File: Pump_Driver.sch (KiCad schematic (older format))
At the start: 6 parts

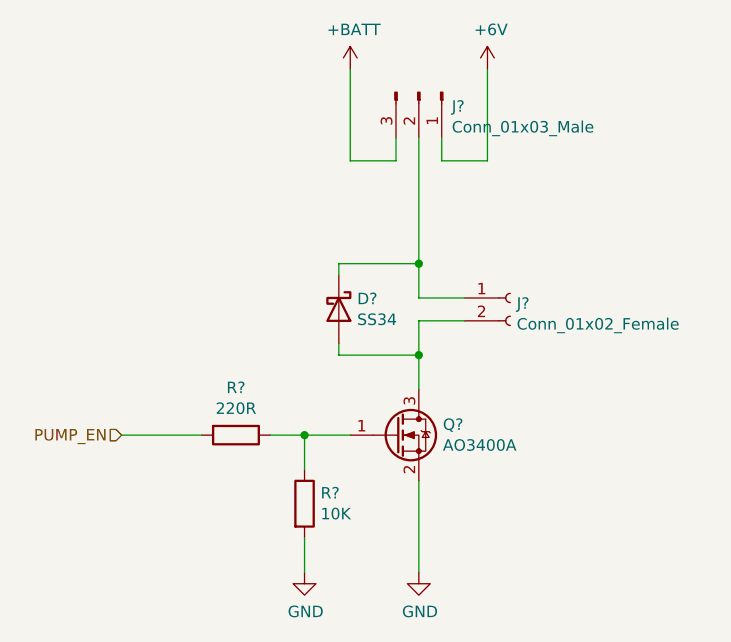
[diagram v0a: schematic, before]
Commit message: Add MPPT battery charger and polyfuse, replace reverse polarity
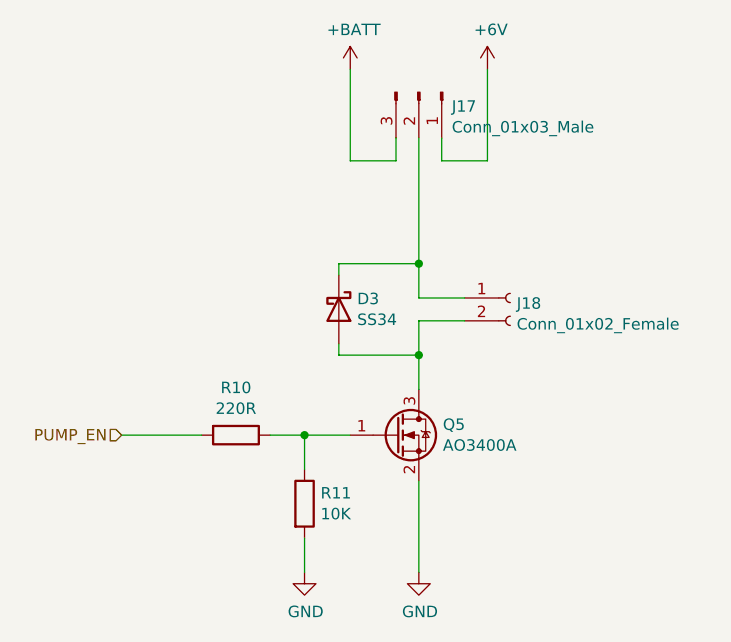
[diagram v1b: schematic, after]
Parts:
- gave numbers to parts that had none: 6
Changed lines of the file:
@@
 PUMP_EN
 $Comp
-L Transistor_FET:AO3400A Q?
+L Transistor_FET:AO3400A Q5
 U 1 1 60BE5370
 P 5950 4250
-F 0 "Q?" H 6155 4296 50  0000 L CNN
+F 0 "Q5" H 6155 4296 50  0000 L CNN
 F 1 "AO3400A" H 6155 4205 50  0000 L CNN
 F 2 "Package_TO_SOT_SMD:SOT-23" H 6150 4175 50  0001 L CIN
@@
 $EndComp
 $Comp
-L Device:R R?
+L Device:R R10
 U 1 1 60BEC7F4
 P 5250 4250
-F 0 "R?" V 5043 4250 50  0000 C CNN
+F 0 "R10" V 5043 4250 50  0000 C CNN
 F 1 "220R" V 5134 4250 50  0000 C CNN
 F 2 "" V 5180 4250 50  0001 C CNN
@@
 	5400 4250 5550 4250
 $Comp
-L Device:R R?
+L Device:R R11
 U 1 1 60BEDCBD
 P 5550 4550
-F 0 "R?" H 5620 4596 50  0000 L CNN
+F 0 "R11" H 5620 4596 50  0000 L CNN
 F 1 "10K" H 5620 4505 50  0000 L CNN
 F 2 "" V 5480 4550 50  0001 C CNN
@@
 	5550 4250 5750 4250
 $Comp
-L power:GND #PWR?
+L power:GND #PWR039
 U 1 1 60BEE60C
 P 5550 4850
-F 0 "#PWR?" H 5550 4600 50  0001 C CNN
+F 0 "#PWR039" H 5550 4600 50  0001 C CNN
 F 1 "GND" H 5555 4677 50  0000 C CNN
 F 2 "" H 5550 4850 50  0001 C CNN
@@
 	5550 4850 5550 4700
 $Comp
-L power:GND #PWR?
+L power:GND #PWR041
 U 1 1 60BEEC8C
 P 6050 4850
-F 0 "#PWR?" H 6050 4600 50  0001 C CNN
+F 0 "#PWR041" H 6050 4600 50  0001 C CNN
 F 1 "GND" H 6055 4677 50  0000 C CNN
 F 2 "" H 6050 4850 50  0001 C CNN
@@
 	6050 4850 6050 4450
 $Comp
-L Connector:Conn_01x02_Female J?
+L Connector:Conn_01x02_Female J18
 U 1 1 60BF29BF
 P 6450 3650
-F 0 "J?" H 6478 3626 50  0000 L CNN
+F 0 "J18" H 6478 3626 50  0000 L CNN
 F 1 "Conn_01x02_Female" H 6478 3535 50  0000 L CNN
 F 2 "" H 6450 3650 50  0001 C CNN
@@
 $EndComp
 $Comp
-L Connector:Conn_01x03_Male J?
+L Connector:Conn_01x03_Male J17
 U 1 1 60BF35EE
 P 6050 2750
-F 0 "J?" V 6112 2894 50  0000 L CNN
+F 0 "J17" V 6112 2894 50  0000 L CNN
 F 1 "Conn_01x03_Male" V 6203 2894 50  0000 L CNN
 F 2 "" H 6050 2750 50  0001 C CNN
@@
 	6050 3650 6050 3500
 $Comp
-L Device:D_Schottky D?
+L Device:D_Schottky D3
 U 1 1 60BF7F76
 P 5700 3700
-F 0 "D?" V 5654 3780 50  0000 L CNN
+F 0 "D3" V 5654 3780 50  0000 L CNN
 F 1 "SS34" V 5745 3780 50  0000 L CNN
 F 2 "Diode_SMD:D_SMA" H 5700 3700 50  0001 C CNN
@@
 	6050 3900 6050 3750
 $Comp
-L power:+BATT #PWR?
+L power:+BATT #PWR040
 U 1 1 60BFA590
 P 5750 2650
-F 0 "#PWR?" H 5750 2500 50  0001 C CNN
+F 0 "#PWR040" H 5750 2500 50  0001 C CNN
 F 1 "+BATT" H 5765 2823 50  0000 C CNN
 F 2 "" H 5750 2650 50  0001 C CNN
@@
 $EndComp
 $Comp
-L power:+6V #PWR?
+L power:+6V #PWR042
 U 1 1 60BFA941
 P 6350 2650
-F 0 "#PWR?" H 6350 2500 50  0001 C CNN
+F 0 "#PWR042" H 6350 2500 50  0001 C CNN
 F 1 "+6V" H 6365 2823 50  0000 C CNN
 F 2 "" H 6350 2650 50  0001 C CNN

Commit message: Remove all references to 6V supply which has been removed
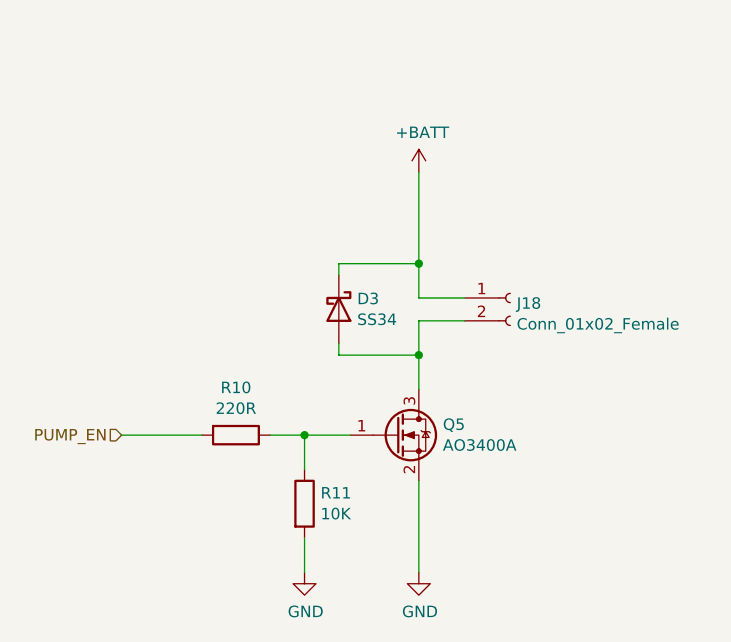
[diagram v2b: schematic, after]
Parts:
- removed J17: Conn_01x03_Male, symbol Connector:Conn_01x03_Male
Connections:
- net +BATT: now also D3.1 (K), J18.1 (Pin_1)
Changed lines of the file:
@@
 	1    0    0    -1
-$EndComp
-$Comp
-L Connector:Conn_01x03_Male J17
-U 1 1 60BF35EE
-P 6050 2750
-F 0 "J17" V 6112 2894 50  0000 L CNN
-F 1 "Conn_01x03_Male" V 6203 2894 50  0000 L CNN
-F 2 "" H 6050 2750 50  0001 C CNN
-F 3 "~" H 6050 2750 50  0001 C CNN
-	1    6050 2750
-	0    1    1    0
 $EndComp
 Wire Wire Line
@@
 Wire Wire Line
 	5700 3550 5700 3500
-Connection ~ 6050 3500
-Wire Wire Line
-	6050 3500 6050 2950
 Wire Wire Line
 	5700 3850 5700 3900
@@
 L power:+BATT #PWR040
 U 1 1 60BFA590
-P 5750 2650
-F 0 "#PWR040" H 5750 2500 50  0001 C CNN
-F 1 "+BATT" H 5765 2823 50  0000 C CNN
-F 2 "" H 5750 2650 50  0001 C CNN
-F 3 "" H 5750 2650 50  0001 C CNN
-	1    5750 2650
-	1    0    0    -1
-$EndComp
-$Comp
-L power:+6V #PWR042
-U 1 1 60BFA941
-P 6350 2650
-F 0 "#PWR042" H 6350 2500 50  0001 C CNN
-F 1 "+6V" H 6365 2823 50  0000 C CNN
-F 2 "" H 6350 2650 50  0001 C CNN
-F 3 "" H 6350 2650 50  0001 C CNN
-	1    6350 2650
+P 6050 3100
+F 0 "#PWR040" H 6050 2950 50  0001 C CNN
+F 1 "+BATT" H 6065 3273 50  0000 C CNN
+F 2 "" H 6050 3100 50  0001 C CNN
+F 3 "" H 6050 3100 50  0001 C CNN
+	1    6050 3100
 	1    0    0    -1
 $EndComp
 Wire Wire Line
-	6150 2950 6150 3050
-Wire Wire Line
-	6150 3050 6350 3050
-Wire Wire Line
-	6350 3050 6350 2650
-Wire Wire Line
-	5750 2650 5750 3050
-Wire Wire Line
-	5750 3050 5950 3050
-Wire Wire Line
-	5950 3050 5950 2950
+	6050 3100 6050 3500
 Wire Wire Line
 	5700 3900 6050 3900
 Wire Wire Line
 	5700 3500 6050 3500
+Connection ~ 6050 3500
 $EndSCHEMATC

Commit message: Finalize schematic
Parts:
- removed J18: Conn_01x02_Female, symbol Connector:Conn_01x02_Female
- added J?: Conn_01x02, Connector_JST:JST_XH_S2B-XH-A_1x02_P2.50mm_Horizontal, symbol Connector_Generic:Conn_01x02
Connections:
- net +BATT: now also J?.1 (Pin_1)
- net at D3.2 (A), Q5.3 (D): now also J?.2 (Pin_2)
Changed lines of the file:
@@
 Wire Wire Line
 	6050 4850 6050 4450
-$Comp
-L Connector:Conn_01x02_Female J18
-U 1 1 60BF29BF
-P 6450 3650
-F 0 "J18" H 6478 3626 50  0000 L CNN
-F 1 "Conn_01x02_Female" H 6478 3535 50  0000 L CNN
-F 2 "" H 6450 3650 50  0001 C CNN
-F 3 "~" H 6450 3650 50  0001 C CNN
-	1    6450 3650
-	1    0    0    -1
-$EndComp
 Wire Wire Line
 	6050 4050 6050 3900
@@
 	5700 3500 6050 3500
 Connection ~ 6050 3500
+$Comp
+L Connector_Generic:Conn_01x02 J?
+U 1 1 60D4F94A
+P 6450 3650
+F 0 "J?" H 6530 3642 50  0000 L CNN
+F 1 "Conn_01x02" H 6530 3551 50  0000 L CNN
+F 2 "Connector_JST:JST_XH_S2B-XH-A_1x02_P2.50mm_Horizontal" H 6450 3650 50  0001 C CNN
+F 3 "~" H 6450 3650 50  0001 C CNN
+	1    6450 3650
+	1    0    0    -1
+$EndComp
 $EndSCHEMATC

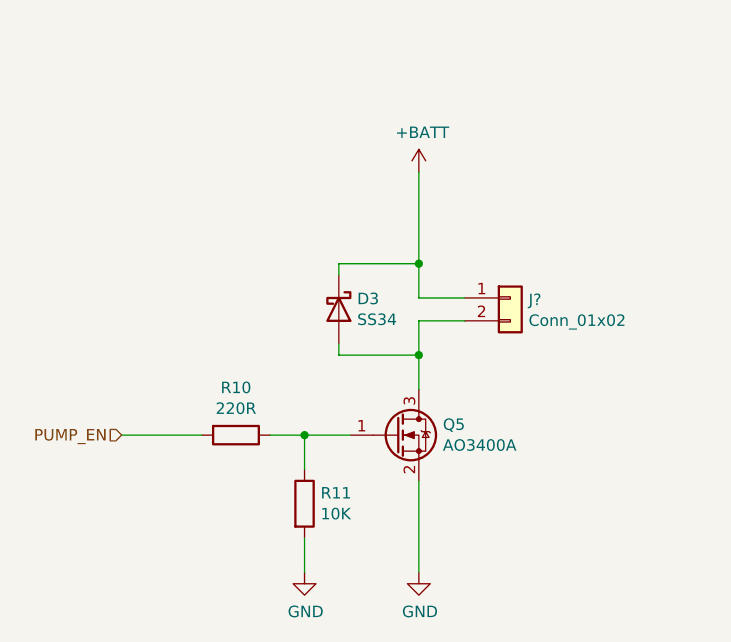
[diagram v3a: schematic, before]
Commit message: Finish routing of Rev 1
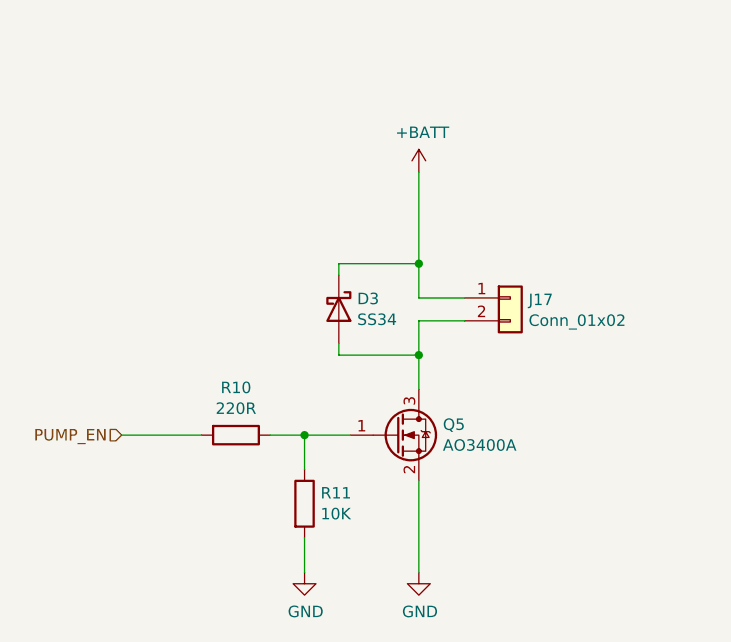
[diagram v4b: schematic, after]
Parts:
- J17: renamed from J?; footprint Connector_JST:JST_XH_S2B-XH-A_1x02_P2.50mm_Horizontal -> Connector_JST:JST_XH_B2B-XH-AM_1x02_P2.50mm_Vertical
- Q5: LCSC (none) -> C20917
- R10, R11: footprint (none) -> Resistor_SMD:R_0603_1608Metric
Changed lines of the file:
@@
 $Descr A4 11693 8268
 encoding utf-8
-Sheet 9 9
+Sheet 9 10
 Title ""
 Date ""
@@
 F 2 "Package_TO_SOT_SMD:SOT-23" H 6150 4175 50  0001 L CIN
 F 3 "http://www.aosmd.com/pdfs/datasheet/AO3400A.pdf" H 5950 4250 50  0001 L CNN
+F 4 "C20917" H 5950 4250 50  0001 C CNN "LCSC"
 	1    5950 4250
 	1    0    0    -1
@@
 F 0 "R10" V 5043 4250 50  0000 C CNN
 F 1 "220R" V 5134 4250 50  0000 C CNN
-F 2 "" V 5180 4250 50  0001 C CNN
+F 2 "Resistor_SMD:R_0603_1608Metric" V 5180 4250 50  0001 C CNN
 F 3 "~" H 5250 4250 50  0001 C CNN
 	1    5250 4250
@@
 F 0 "R11" H 5620 4596 50  0000 L CNN
 F 1 "10K" H 5620 4505 50  0000 L CNN
-F 2 "" V 5480 4550 50  0001 C CNN
+F 2 "Resistor_SMD:R_0603_1608Metric" V 5480 4550 50  0001 C CNN
 F 3 "~" H 5550 4550 50  0001 C CNN
 	1    5550 4550
@@
 Connection ~ 6050 3500
 $Comp
-L Connector_Generic:Conn_01x02 J?
+L Connector_Generic:Conn_01x02 J17
 U 1 1 60D4F94A
 P 6450 3650
-F 0 "J?" H 6530 3642 50  0000 L CNN
+F 0 "J17" H 6530 3642 50  0000 L CNN
 F 1 "Conn_01x02" H 6530 3551 50  0000 L CNN
-F 2 "Connector_JST:JST_XH_S2B-XH-A_1x02_P2.50mm_Horizontal" H 6450 3650 50  0001 C CNN
+F 2 "Connector_JST:JST_XH_B2B-XH-AM_1x02_P2.50mm_Vertical" H 6450 3650 50  0001 C CNN
 F 3 "~" H 6450 3650 50  0001 C CNN
 	1    6450 3650
